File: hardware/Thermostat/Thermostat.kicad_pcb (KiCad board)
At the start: 2 copper layers, 106 x 75 mm, 45 parts, among them J1 MainConnectorr, J2 Screw_Terminal_01x02, J3 AVR-ISP-6, J4 Conn_01x03_Pin, J5 Conn_01x03_Pin, K1 G6E, K2 G6E, K3 G6E, K4 G6E, SW1_UP1 SW_Push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

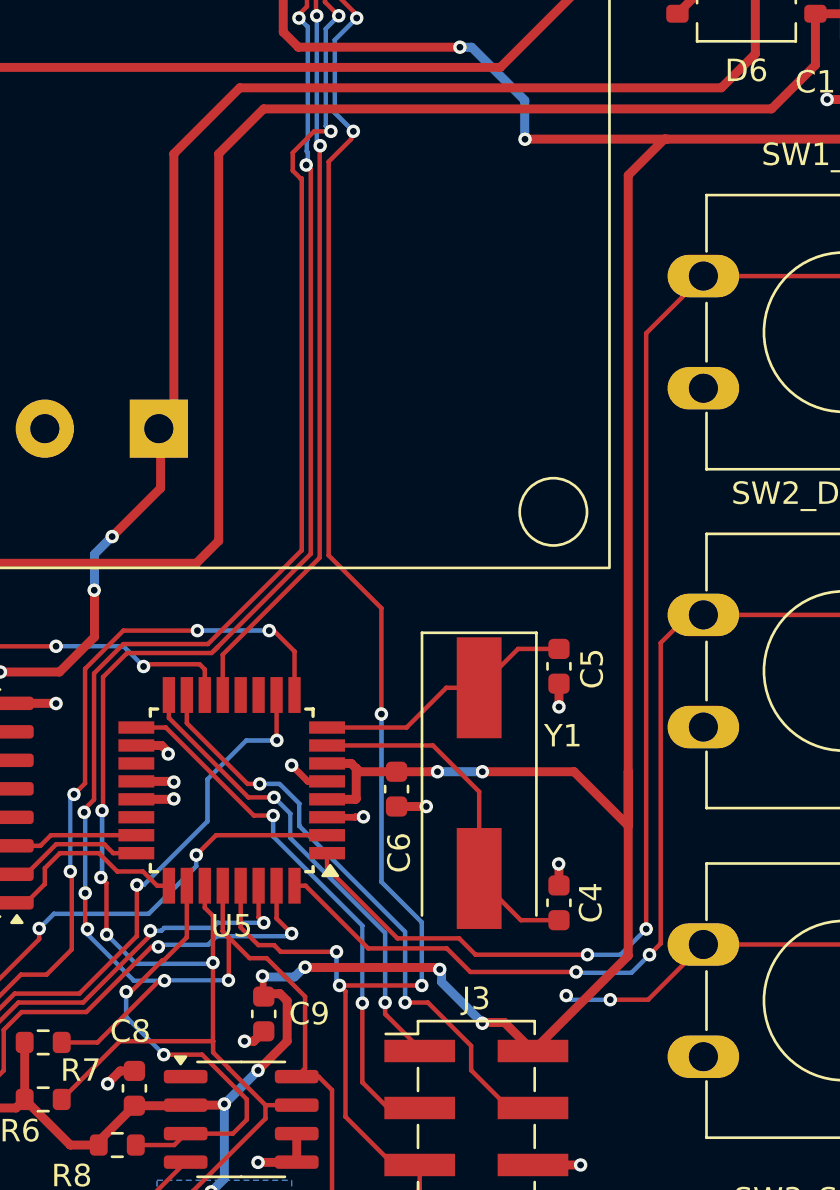
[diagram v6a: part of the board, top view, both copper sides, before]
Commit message: Select button routing
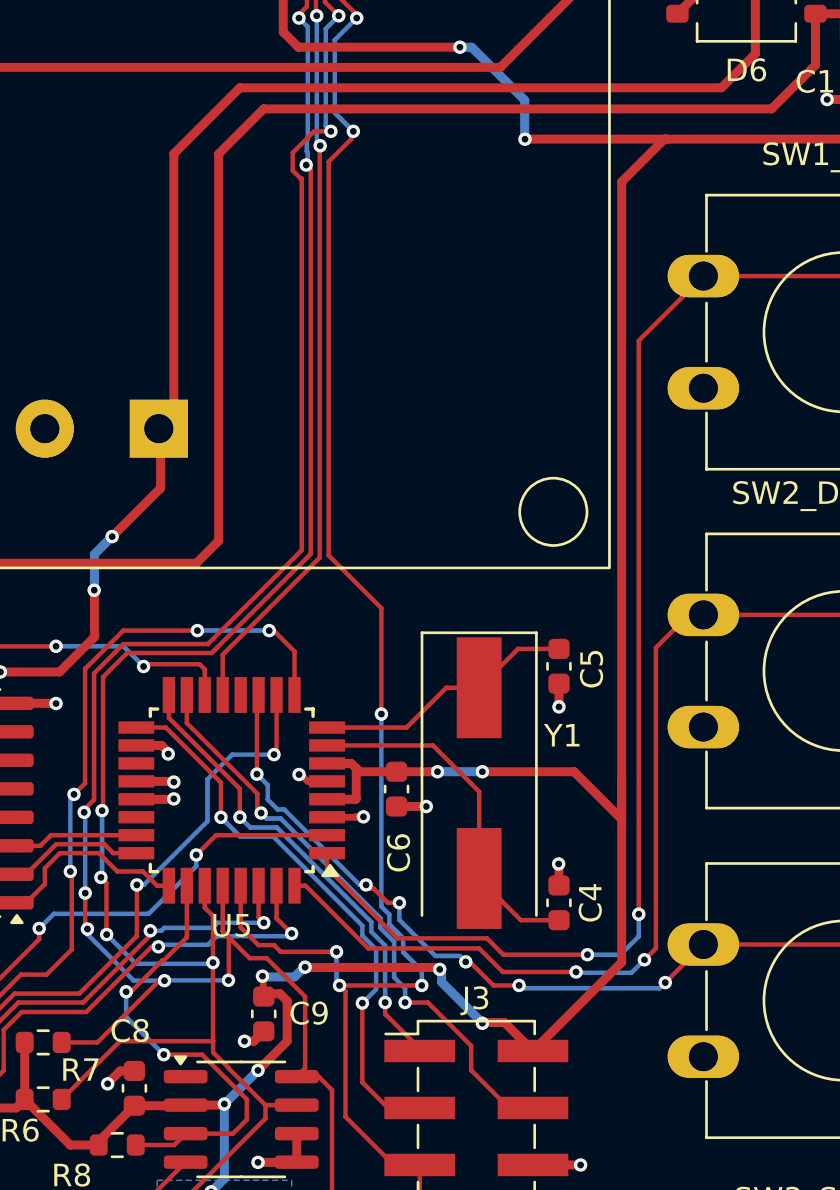
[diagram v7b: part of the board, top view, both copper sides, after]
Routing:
- net Net-(U5-PD7): track 19.8 -> 41.5 mm, vias 2 -> 6
- net +5V: track 199.4 -> 198.4 mm
- net Net-(J3-SCK): track 24.3 -> 25.2 mm
- net GND: track 50.0 -> 49.5 mm

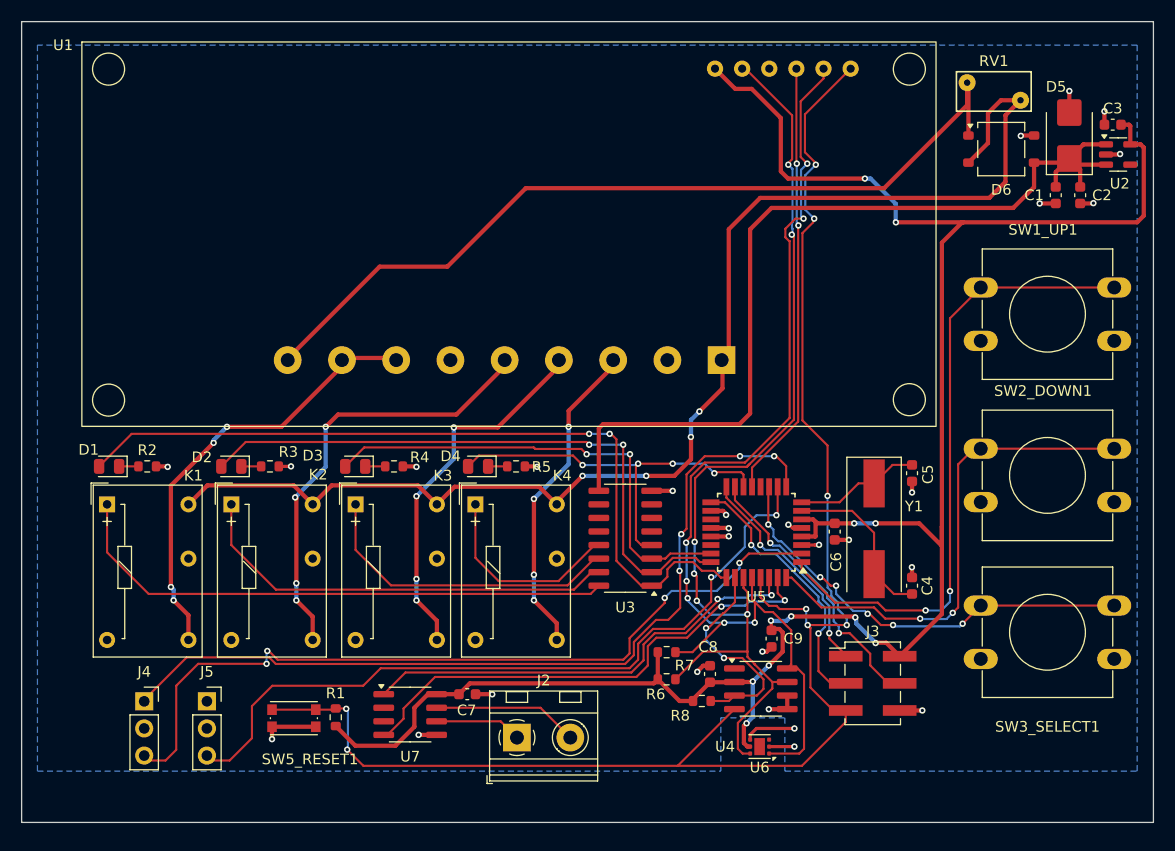
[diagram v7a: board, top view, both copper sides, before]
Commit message: Lots of work on JLCPCB parts
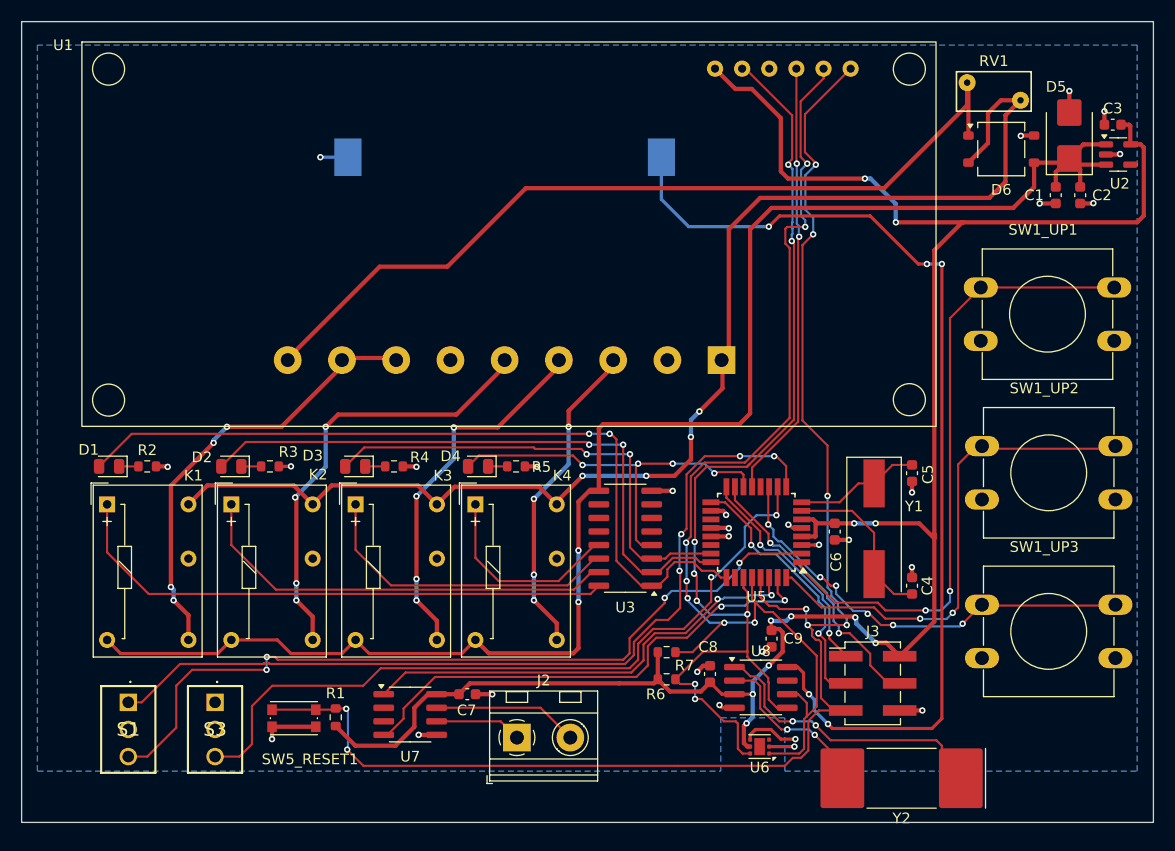
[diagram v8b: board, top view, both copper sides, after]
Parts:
- removed J4, J5: Conn_01x03_Pin, Connector_PinSocket_2.54mm:PinSocket_1x03_P2.54mm_Vertical
- removed R8: 5k, Resistor_SMD:R_0603_1608Metric
- removed SW2_DOWN1, SW3_SELECT1: SW_Push, Button_Switch_THT:SW_PUSH-12mm
- removed U4: DS3232M, Package_SO:SOIC-8_3.9x4.9mm_P1.27mm
- added BT1: Battery_Cell, Battery:BatteryHolder_Keystone_1058_1x2032, B.Cu at (162.8, 63.5)
- added S1: 2MS3T1B1M2QES, ThermostatFootprints:2MS1T1B1M2QES, F.Cu at (127.5, 114.6)
- added S3: 2MS1T1B1M2QES, ThermostatFootprints:2MS1T1B1M2QES, F.Cu at (135.6, 114.6)
- added SW1_UP2: SW_Push, Button_Switch_THT:SW_PUSH-12mm, F.Cu at (207.5, 90.6)
- added SW1_UP3: SW_Push, Button_Switch_THT:SW_PUSH-12mm, F.Cu at (207.5, 105.4)
- added U8: DS1307Z+, Package_SO:SOIC-8_3.9x4.9mm_P1.27mm, F.Cu at (186.8, 113.2)
- added Y2: Crystal, Crystal:Crystal_SMD_SeikoEpson_MA505-2Pin_12.7x5.1mm, F.Cu at (199.9, 121.7)
- C1: value 10mF -> 10uF
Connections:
- net Net-(U5-PD0) renamed RX0
- net Net-(U5-PD1) renamed TX0
- K1 pad 6: GND -> 24VDC
- K2 pad 6: GND -> 24VDC
- K3 pad 6: GND -> 24VDC
- K4 pad 6: GND -> 24VDC
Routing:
- net +BATT: track 0.00 -> 95.2 mm, vias 0 -> 5
- net 24VDC: track 85.8 -> 149.8 mm, vias 0 -> 2
- net Net-(U8-X1): track 0.00 -> 27.5 mm, vias 0 -> 2
- net RTC_INT: track 20.4 -> 0.00 mm, vias 2 -> 0
- net Net-(U8-X2): track 0.00 -> 16.0 mm, vias 0 -> 2
- net ^RESET: track 147.7 -> 141.3 mm
- net I2C_SDA: track 93.2 -> 98.6 mm, vias 6 -> 8
- net I2C_SCL: track 96.9 -> 101.1 mm
- net +5V: track 198.4 -> 195.7 mm
- net GND: track 49.5 -> 51.0 mm, vias 28 -> 29
- net Net-(S1-NC): track 76.5 -> 75.6 mm
